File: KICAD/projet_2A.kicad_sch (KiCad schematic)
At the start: 0 parts

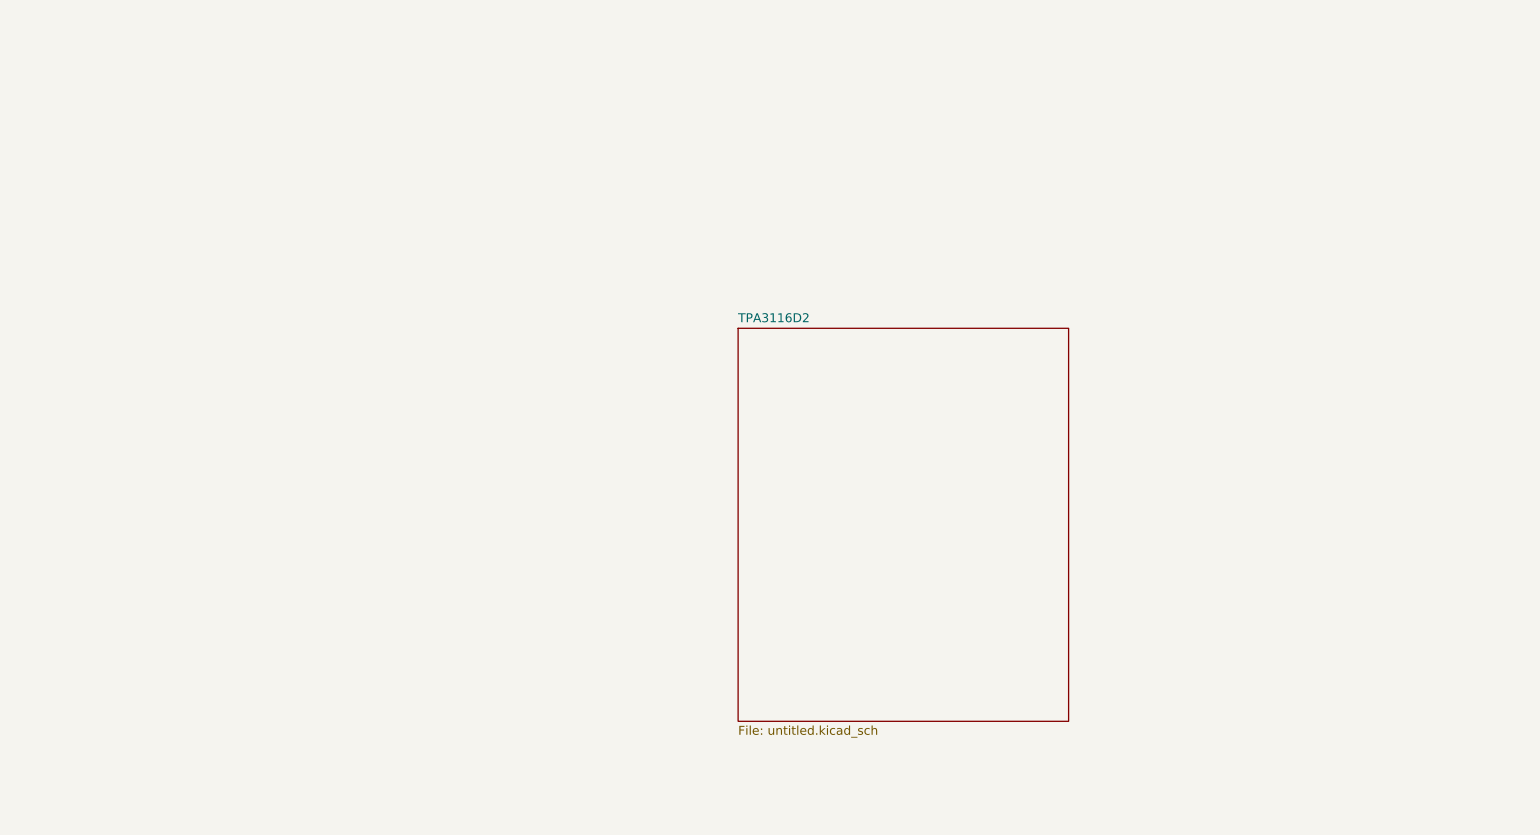
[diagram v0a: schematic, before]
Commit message: Ajout footprint
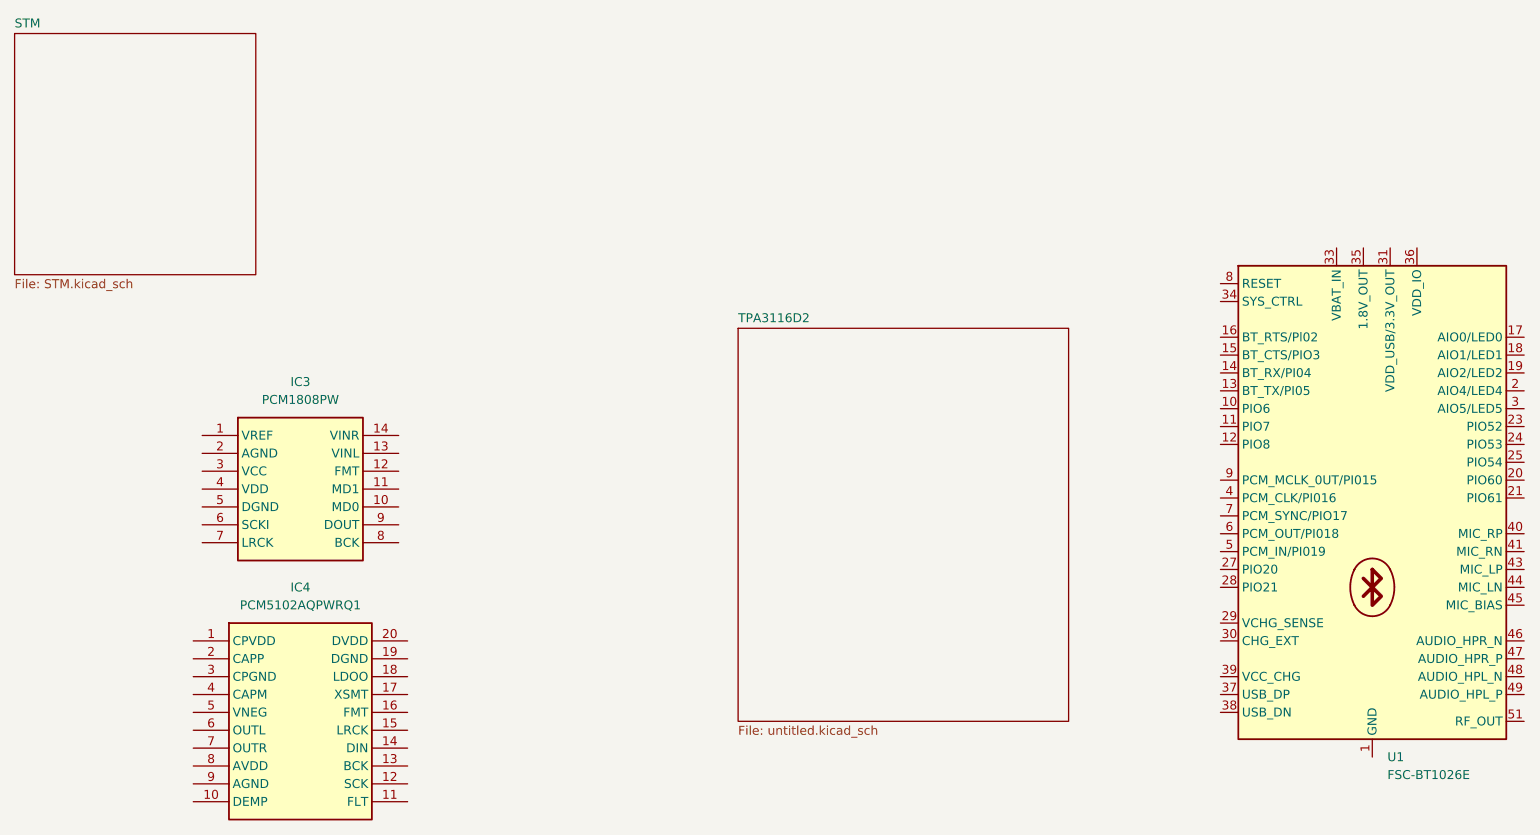
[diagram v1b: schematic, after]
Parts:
- added IC3: PCM1808PW, Package_SO:TSSOP-14_4.4x5mm_P0.65mm, symbol PCM1808PW:PCM1808PW
- added IC4: PCM5102AQPWRQ1, Package_SO:TSSOP-20_4.4x6.5mm_P0.65mm, symbol PCM5102AQPWRQ1:PCM5102AQPWRQ1
- added U1: FSC-BT1026E, Bluetooth:FSC-BT1026x, symbol Bluetooth_FSC_BT1026x:FSC-BT1026x
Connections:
- new net: U1.1 (GND), U1.22 (GND), U1.32 (GND), U1.50 (GND), U1.52 (GND)
- new net: U1.26 (NC), U1.42 (NC)
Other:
- added sheet STM (STM.kicad_sch)

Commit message: BT + PCM1808
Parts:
- removed IC3: PCM1808PW, Package_SO:TSSOP-14_4.4x5mm_P0.65mm, symbol PCM1808PW:PCM1808PW
- removed U1: FSC-BT1026E, Bluetooth:FSC-BT1026x, symbol Bluetooth_FSC_BT1026x:FSC-BT1026x
- added J1: AudioJack3_Ground_Switch, symbol Connector_Audio:AudioJack3_Ground_Switch
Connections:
- new net Bluetooth/AUDIO_HPL_P: J1.TN
- new net Bluetooth/AUDIO_HPR_P: J1.RN
- new net GND: J1.S
- new net JACK_DET: J1.G
- new net R/VINR: J1.R
- new net T/VINL: J1.T
- no-connect marks 0 -> 1
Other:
- added sheet ADC_PCM1808 (ADC.kicad_sch)
- added sheet Bluetooth (bluetooth.kicad_sch)
- sheet STM ports: added JACK_DET, SAI1_FS_A/LRCK, SAI1_MCLK_A/SCKI, SAI1_SCK_A/BCK, SAI1_SD_A/DOUT, USART_RX, USART_TX; removed none
- moved on the sheet: IC4

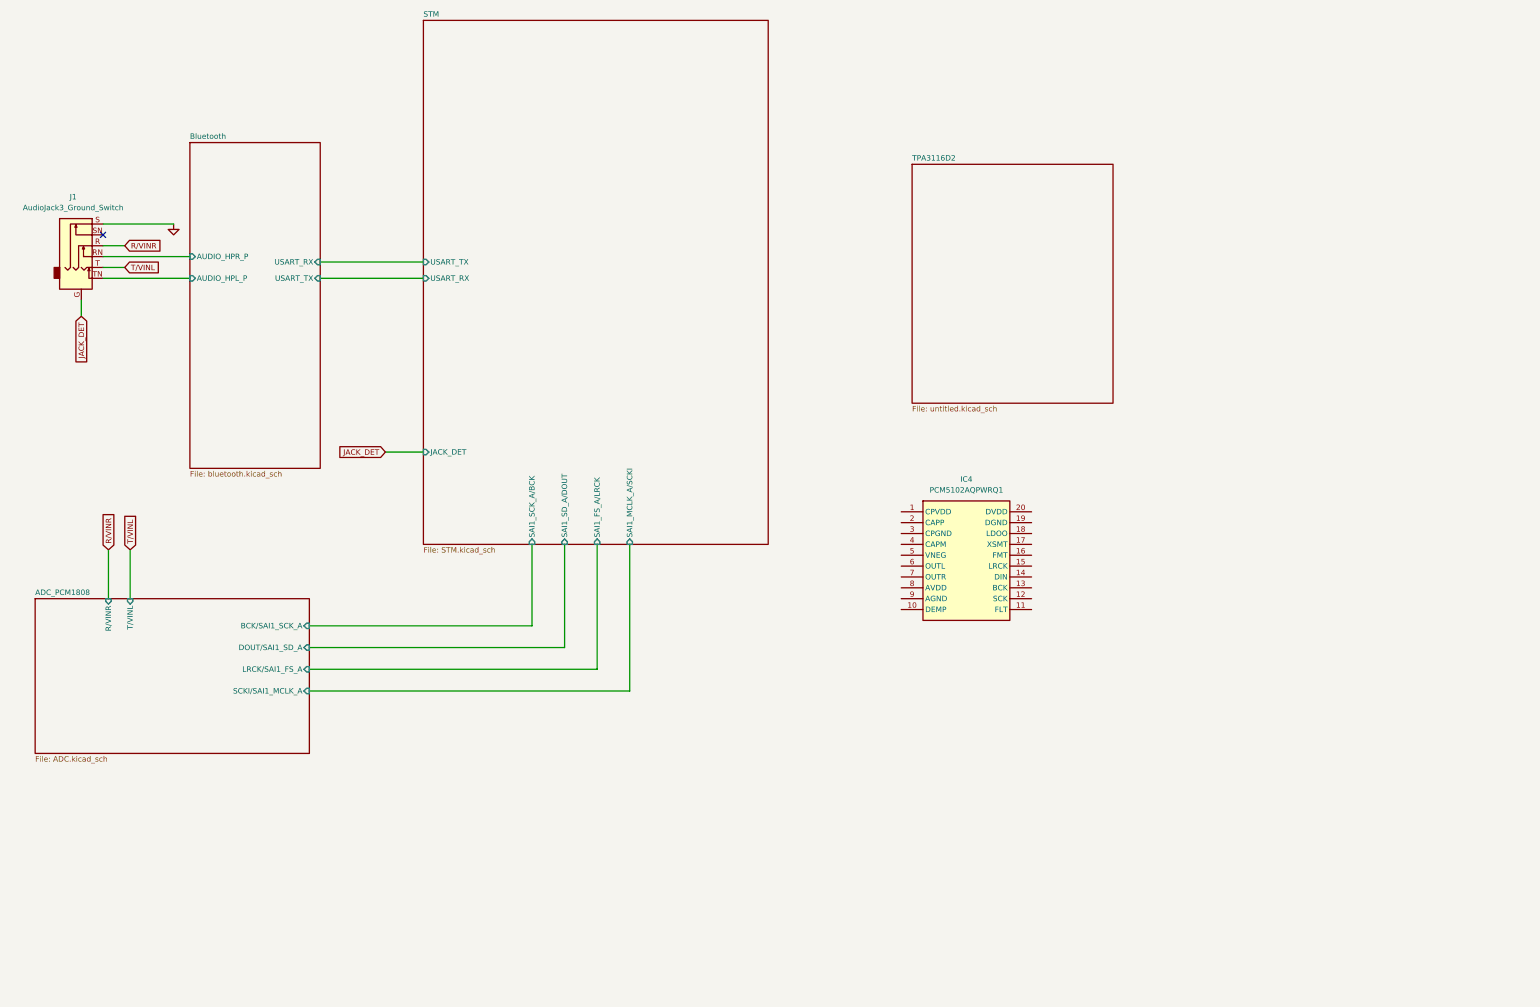
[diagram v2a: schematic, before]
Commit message: Config ports DAC + Ampli
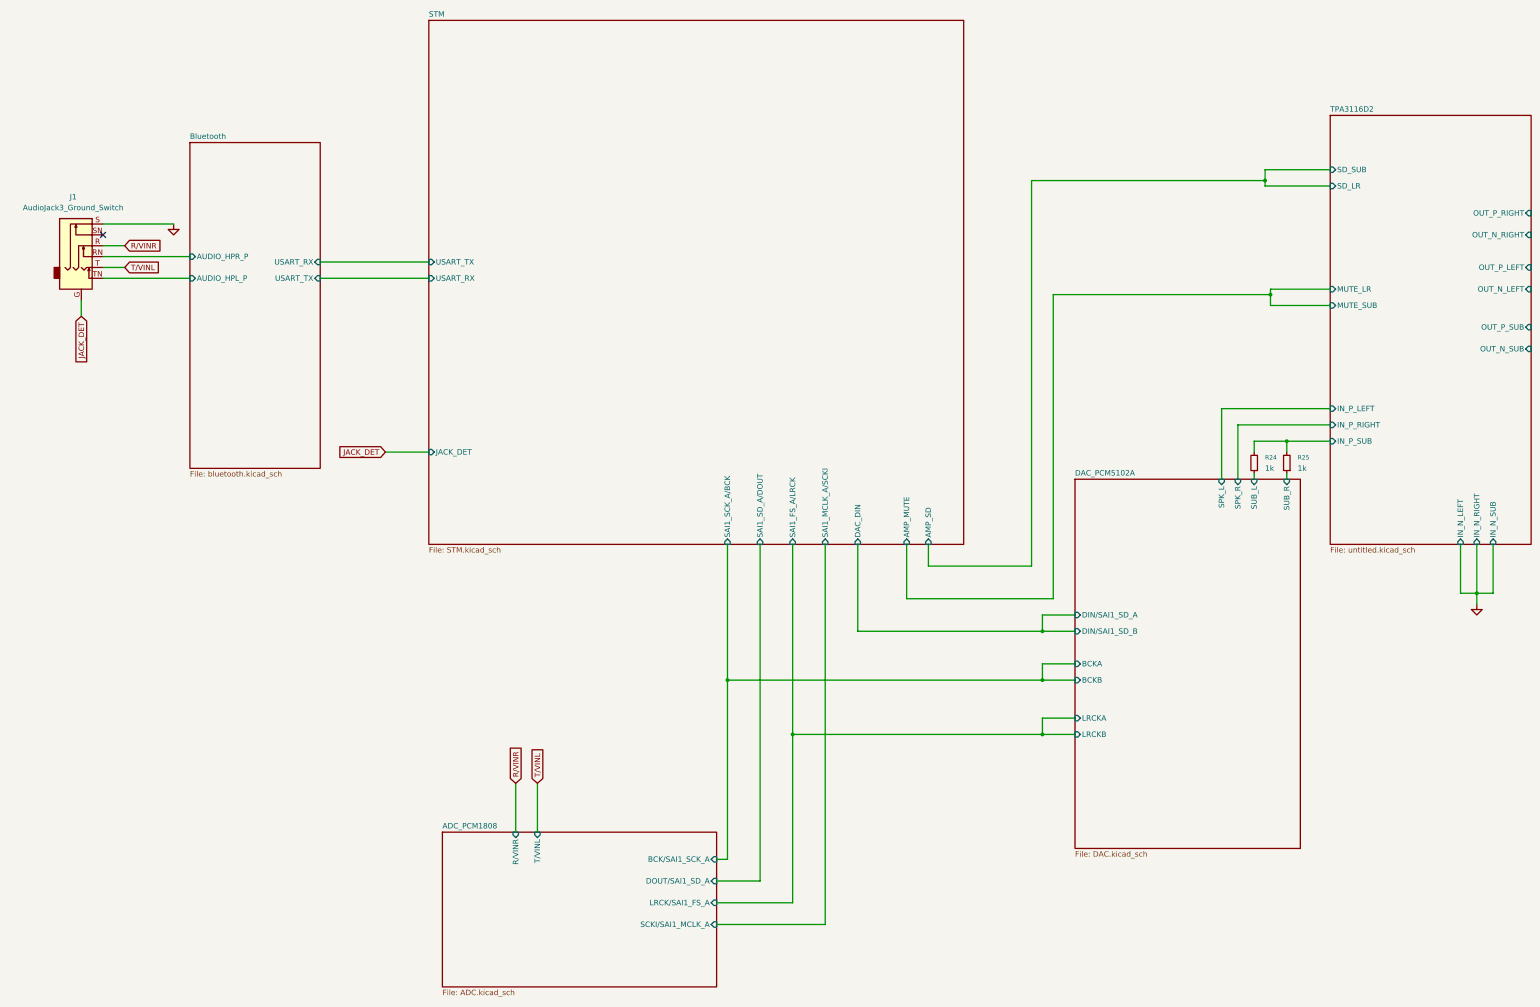
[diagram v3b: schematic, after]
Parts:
- removed IC4: PCM5102AQPWRQ1, Package_SO:TSSOP-20_4.4x6.5mm_P0.65mm, symbol PCM5102AQPWRQ1:PCM5102AQPWRQ1
- added R24, R25: 1k, symbol Device:R_Small
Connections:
- new net DAC_PCM5102A/SUB_L: R24.1
- new net DAC_PCM5102A/SUB_R: R25.1
- new net TPA3116D2/IN_P_SUB: R24.2, R25.2
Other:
- added sheet DAC_PCM5102A (DAC.kicad_sch)
- sheet STM ports: added AMP_MUTE, AMP_SD, DAC_DIN; removed none
- sheet TPA3116D2 ports: added IN_N_LEFT, IN_N_RIGHT, IN_N_SUB, IN_P_LEFT, IN_P_RIGHT, IN_P_SUB, MUTE_LR, MUTE_SUB, OUT_N_LEFT, OUT_N_RIGHT, OUT_N_SUB, OUT_P_LEFT, OUT_P_RIGHT, OUT_P_SUB, SD_LR, SD_SUB; removed none
